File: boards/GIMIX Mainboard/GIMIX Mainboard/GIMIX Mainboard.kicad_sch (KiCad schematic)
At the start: 21 parts, among them SW1 SW_DIP_x10, SW2 SW_DIP_x10, U1 74LS640, U10 74LS136, U11 74LS136, U12 74LS00, U13 74LS121, U2 74LS240, U3 74LS240, U4 74LS240, U5 74LS240, U7 74LS138, U8 74LS136, U9 74LS136

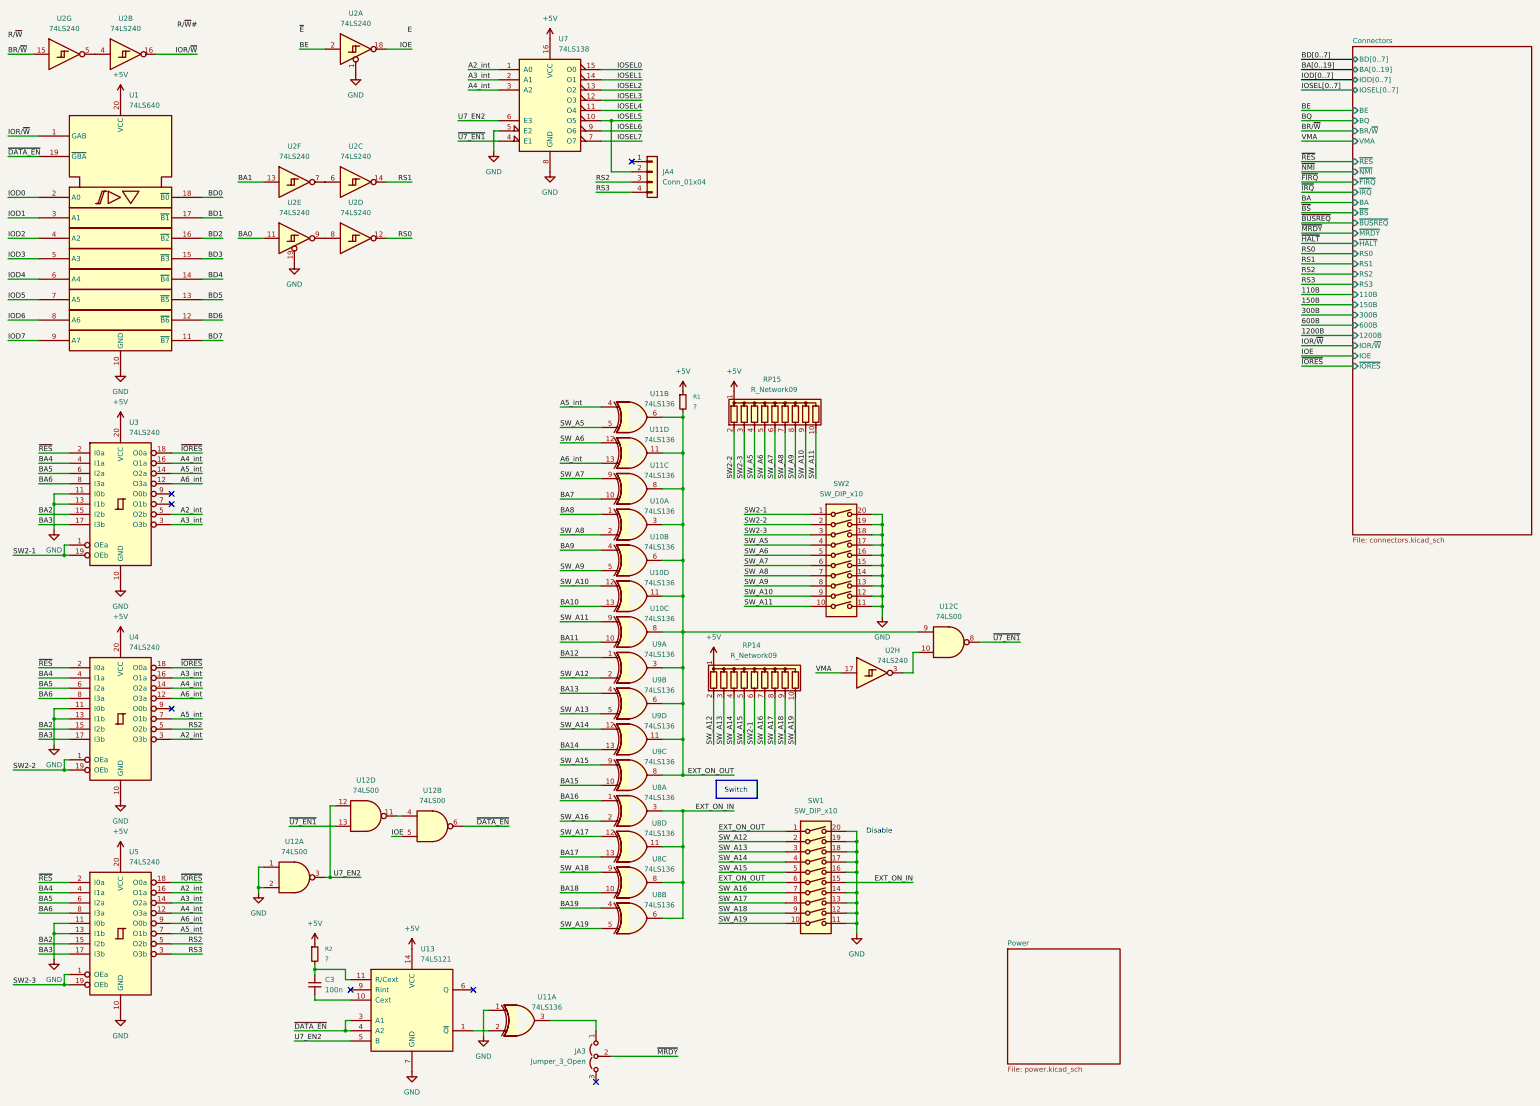
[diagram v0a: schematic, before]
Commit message: motherboard new version silkscreen added
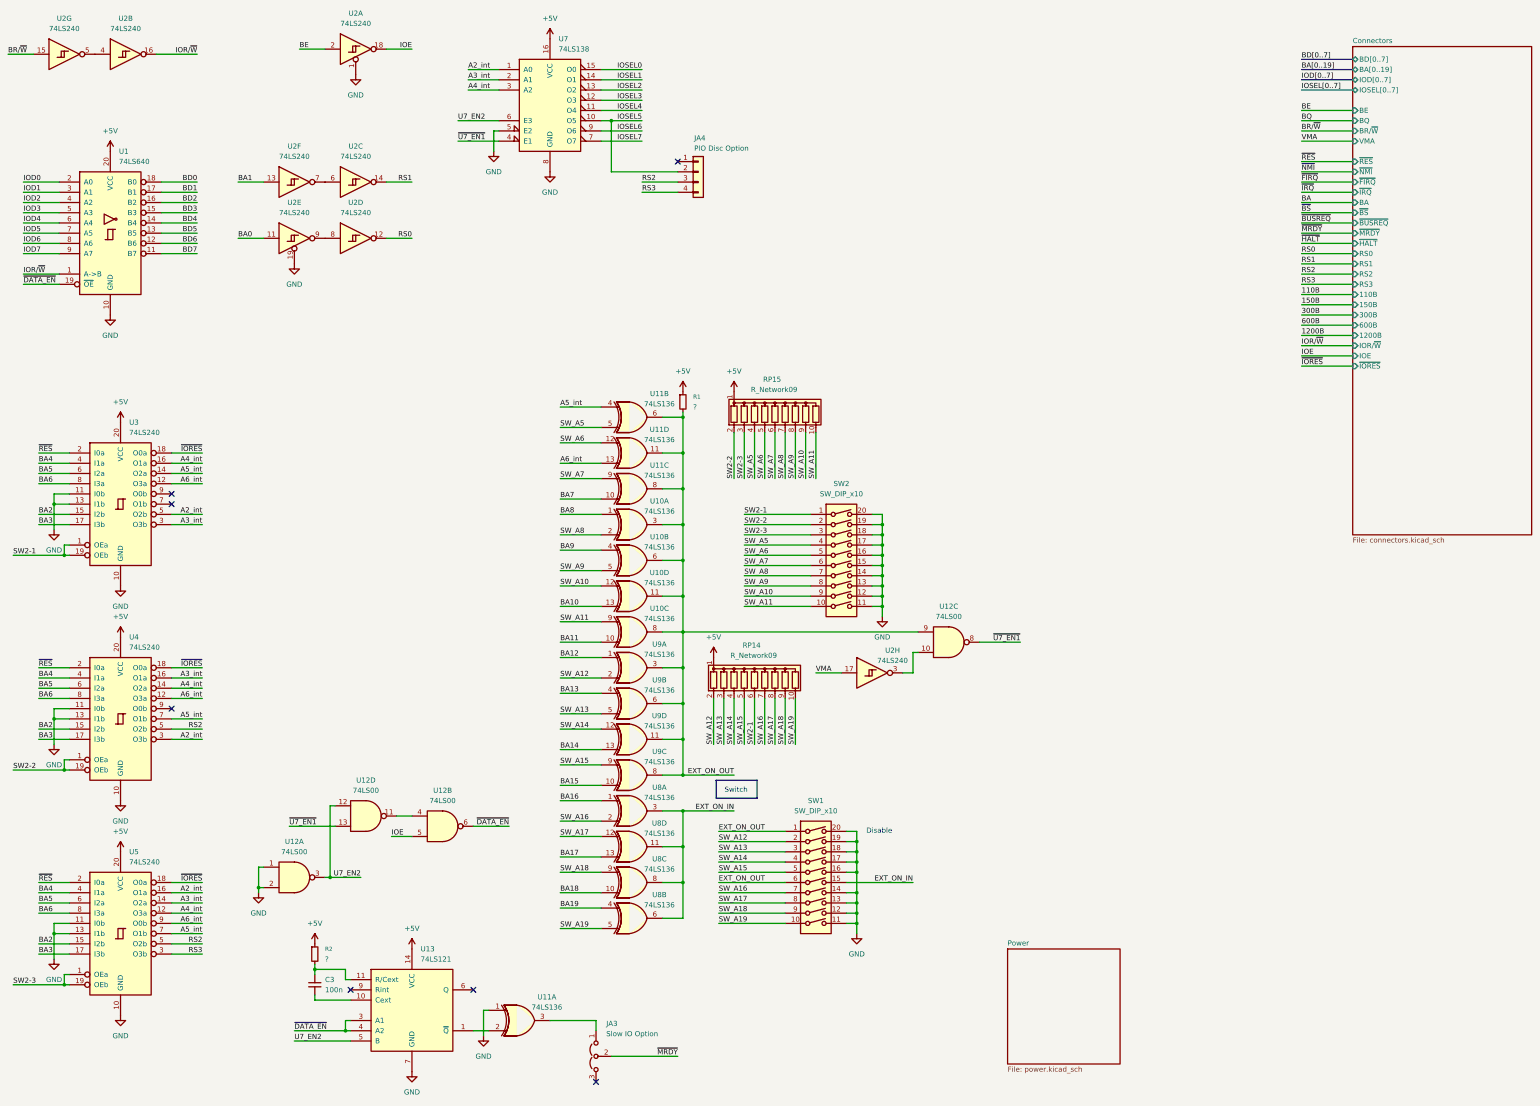
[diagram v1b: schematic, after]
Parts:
- removed U1: 74LS640, Package_DIP:DIP-20_W7.62mm, symbol 74xx_IEEE:74LS640
- added U1: 74LS640, Package_DIP:DIP-20_W7.62mm, symbol my_ics_new:74LS640_small
- JA3: value Jumper_3_Open -> Slow IO Option
- JA4: value Conn_01x04 -> PIO Disc Option
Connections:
- net +5V: now also U1.20 (VCC)
- net BD0: now also U1.18 (B0)
- net BD1: now also U1.17 (B1)
- net BD2: now also U1.16 (B2)
- net BD3: now also U1.15 (B3)
- net BD4: now also U1.14 (B4)
- net BD5: now also U1.13 (B5)
- net BD6: now also U1.12 (B6)
- net BD7: now also U1.11 (B7)
- net GND: now also U1.10 (GND)
- net IOD0: now also U1.2 (A0)
- net IOD1: now also U1.3 (A1)
- net IOD2: now also U1.4 (A2)
- net IOD3: now also U1.5 (A3)
- net IOD4: now also U1.6 (A4)
- net IOD5: now also U1.7 (A5)
- net IOD6: now also U1.8 (A6)
- net IOD7: now also U1.9 (A7)
- net IOR/~{W}: now also U1.1 (A->B)
- net ~{DATA_EN}: now also U1.19 (~{OE})
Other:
- moved on the sheet: JA4, U12B
